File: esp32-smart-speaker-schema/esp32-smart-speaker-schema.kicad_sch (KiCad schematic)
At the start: 15 parts, among them U2 MAX98357A

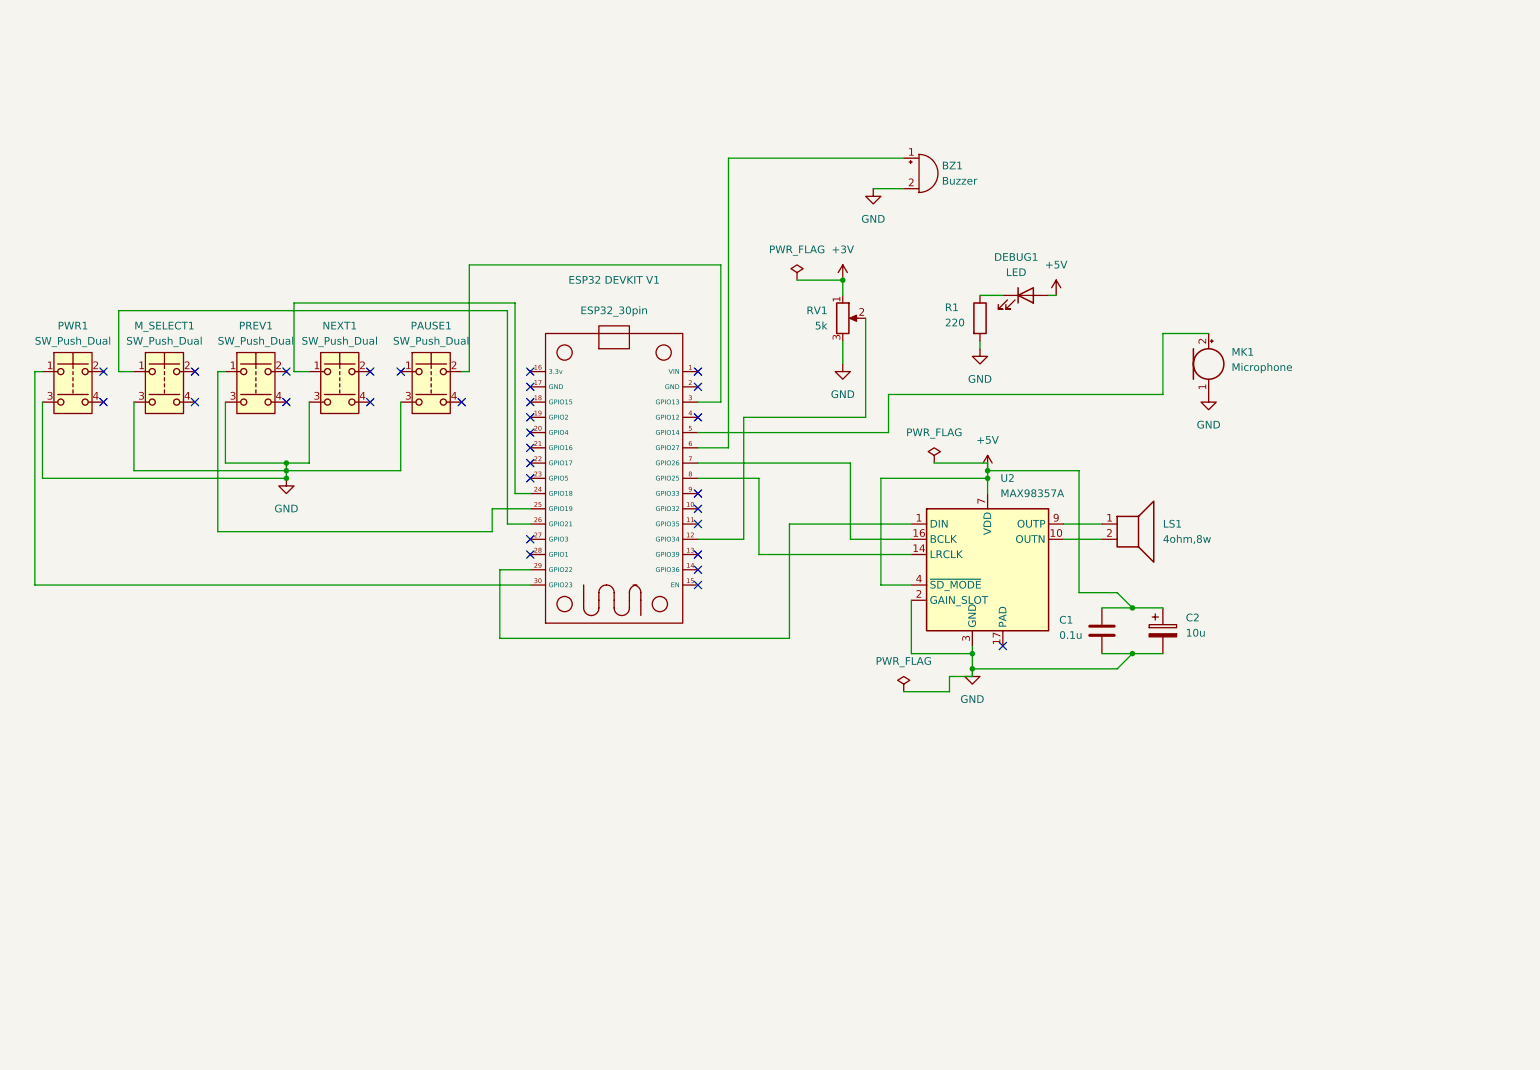
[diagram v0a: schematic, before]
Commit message: Add audio and BLE management features
- Implement AudioManager class for audio control including volume management and sound playback.
- Create BLEManager for battery level monitoring and BLE characteristics.
- Develop Speaker class to manage speaker modes and Bluetooth connections.
- Introduce Buttons handling for power and track navigation.
- Set up PreferencesManager for saving and retrieving volume settings.
- Establish WebServer for serving files and handling HTTP requests for playback control and metadata.
- Implement WiFiManager for connecting to Wi-Fi networks and managing access points.
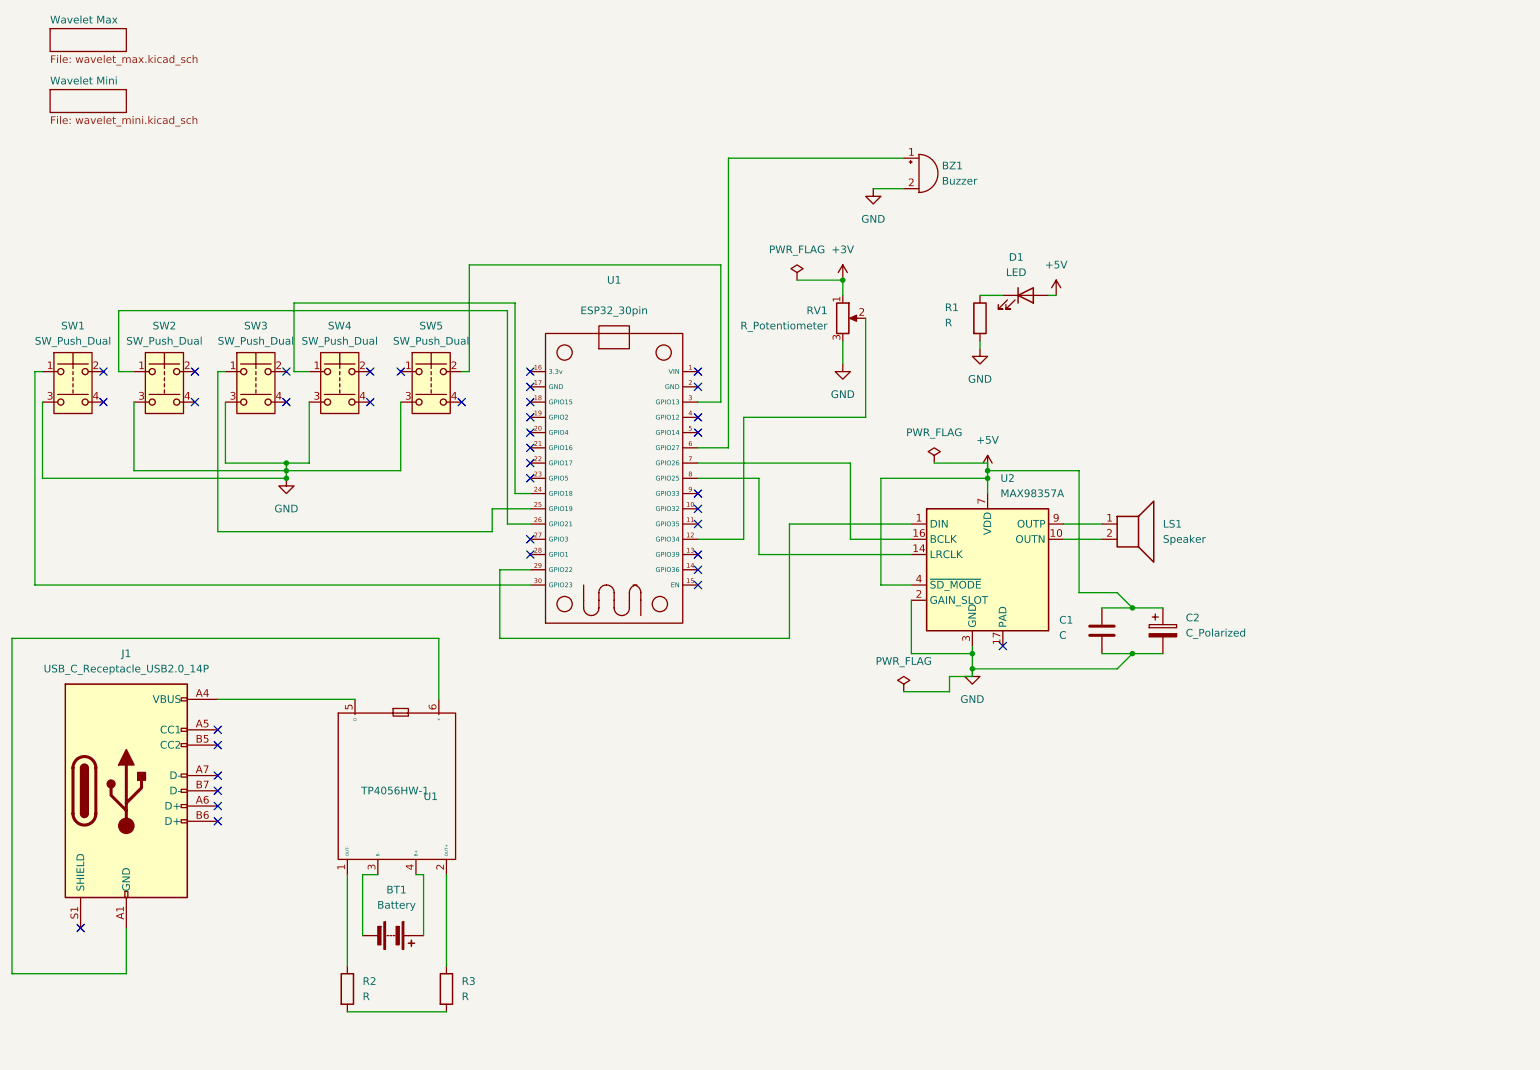
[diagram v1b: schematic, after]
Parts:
- removed MK1: Microphone, symbol Device:Microphone
- added BT1: Battery, symbol Device:Battery
- added J1: USB_C_Receptacle_USB2.0_14P, symbol Connector:USB_C_Receptacle_USB2.0_14P
- added R2, R3: R, symbol Device:R
- added TP4056HW-1: U1, symbol added_by_me:TP4056_HW-373
- C1: value 0.1u -> C
- C2: value 10u -> C_Polarized
- LS1: value 4ohm,8w -> Speaker
- R1: value 220 -> R
- RV1: value 5k -> R_Potentiometer
- U1: renamed from ESP32 DEVKIT V1
- renumbered DEBUG1 to D1, PWR1 to SW1, M_SELECT1 to SW2, PREV1 to SW3, NEXT1 to SW4, PAUSE1 to SW5
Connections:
- new net: R2.1, TP4056HW-1.1 (OUT-)
- new net: R2.2, R3.2
- new net: BT1.1 (+), TP4056HW-1.4 (B+)
- new net: BT1.2 (-), TP4056HW-1.3 (B-)
- new net: R3.1, TP4056HW-1.2 (OUT+)
- new net: J1.A1 (GND), J1.A12 (GND), J1.B1 (GND), J1.B12 (GND), TP4056HW-1.6 (+)
- new net: J1.A4 (VBUS), J1.A9 (VBUS), J1.B4 (VBUS), J1.B9 (VBUS), TP4056HW-1.5 (D)
- no-connect marks 30 -> 38
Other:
- added sheet Wavelet Max (wavelet_max.kicad_sch)
- added sheet Wavelet Mini (wavelet_mini.kicad_sch)

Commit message: Fixed a few bugs for the Wavelet Regular and Max Refactored Codebase
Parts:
- R1: value R -> 220
- R2, R3: value R -> 10k
- SW1: value SW_Push_Dual -> PWR_BTN
- SW2: value SW_Push_Dual -> MODE_BTN
- SW3: value SW_Push_Dual -> PREV_BTN
- SW4: value SW_Push_Dual -> NXT_BTN
- SW5: value SW_Push_Dual -> PAUS-BTN
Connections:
- net GND: now also R2.1, R3.1, TP4056HW-1.1 (OUT-), TP4056HW-1.2 (OUT+), U1.1 (VIN), U1.2 (GND)
- net at U1.11 (GPIO35): now also R2.2, R3.2
- no-connect marks 38 -> 35
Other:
- company: (none) -> Semire Designs
- title: (none) -> Wavelet Speaker
- moved on the sheet: BZ1, C1, C2, D1, LS1, R1, R2, R3, RV1, U2

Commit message: Add Spotify controller and wavelet default image header
- Implemented Spotify controller functionality in Spotify.cpp, including methods for playback control, volume adjustment, and device management.
- Created Spotify.h to declare external variables and function prototypes for the Spotify controller.
- Added wavelet_default.h header file for image declaration.
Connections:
- net at R2.2, R3.2, U1.11 (GPIO35): now also RV1.2, U1.12 (GPIO34)
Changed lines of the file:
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@@
+	)
+	(junction
+		(at 138.43 107.95)
+		(diameter 0)
+		(color 0 0 0 0)
 	)
 	(junction
@@
 	)
 	(junction
-		(at 92.71 186.69)
+		(at 138.43 119.38)
 		(diameter 0)
 		(color 0 0 0 0)
@@
 	)
 	(junction
+		(at 83.82 186.69)
+		(diameter 0)
+		(color 0 0 0 0)
+	)
+	(junction
 		(at 66.04 95.25)
 		(diameter 0)
@@
 	(wire
 		(pts
+			(xy 138.43 119.38) (xy 138.43 107.95)
+		)
+		(stroke
+			(width 0)
+			(type default)
+		)
+	)
+	(wire
+		(pts
 			(xy 138.43 119.38) (xy 185.42 119.38)
 		)
@@
 	(wire
 		(pts
+			(xy 83.82 194.31) (xy 138.43 194.31)
+		)
+		(stroke
+			(width 0)
+			(type default)
+		)
+	)
+	(wire
+		(pts
 			(xy 24.13 80.01) (xy 24.13 115.57)
 		)
@@
 	(wire
 		(pts
-			(xy 138.43 119.38) (xy 138.43 107.95)
-		)
-		(stroke
-			(width 0)
-			(type default)
-		)
-	)
-	(wire
-		(pts
 			(xy 55.88 95.25) (xy 66.04 95.25)
 		)
@@
 	(wire
 		(pts
-			(xy 74.93 186.69) (xy 92.71 186.69)
+			(xy 74.93 186.69) (xy 83.82 186.69)
 		)
 		(stroke
@@
 	(wire
 		(pts
-			(xy 137.16 186.69) (xy 137.16 105.41)
+			(xy 138.43 194.31) (xy 138.43 119.38)
 		)
 		(stroke
@@
 	(wire
 		(pts
-			(xy 134.62 105.41) (xy 137.16 105.41)
+			(xy 134.62 105.41) (xy 138.43 105.41)
 		)
 		(stroke
@@
 	(wire
 		(pts
-			(xy 92.71 186.69) (xy 137.16 186.69)
-		)
-		(stroke
-			(width 0)
-			(type default)
-		)
-	)
-	(wire
-		(pts
 			(xy 139.7 97.79) (xy 134.62 97.79)
 		)
@@
 	(wire
 		(pts
+			(xy 83.82 194.31) (xy 83.82 186.69)
+		)
+		(stroke
+			(width 0)
+			(type default)
+		)
+	)
+	(wire
+		(pts
 			(xy 245.11 130.81) (xy 250.19 130.81)
 		)
@@
 	(wire
 		(pts
+			(xy 83.82 186.69) (xy 92.71 186.69)
+		)
+		(stroke
+			(width 0)
+			(type default)
+		)
+	)
+	(wire
+		(pts
 			(xy 143.51 135.89) (xy 143.51 127)
 		)
@@
 		)
 		(stroke
+			(width 0)
+			(type default)
+		)
+	)
+	(wire
+		(pts
+			(xy 138.43 107.95) (xy 138.43 105.41)
+		)
+		(stroke
